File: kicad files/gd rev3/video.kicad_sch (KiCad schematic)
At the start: 51 parts, among them J17 VGA_Micro, J18 vga_SWD, J22 L77HDE15SD1CH4F, SW6 VGA Boot Sel, SW7 VGA RESET, U19 W25Q128JVS, U22 74HCT245, U23 RP2040, U24 74LVC2G04, Y2 ECS-120-18-33-JEM-TR

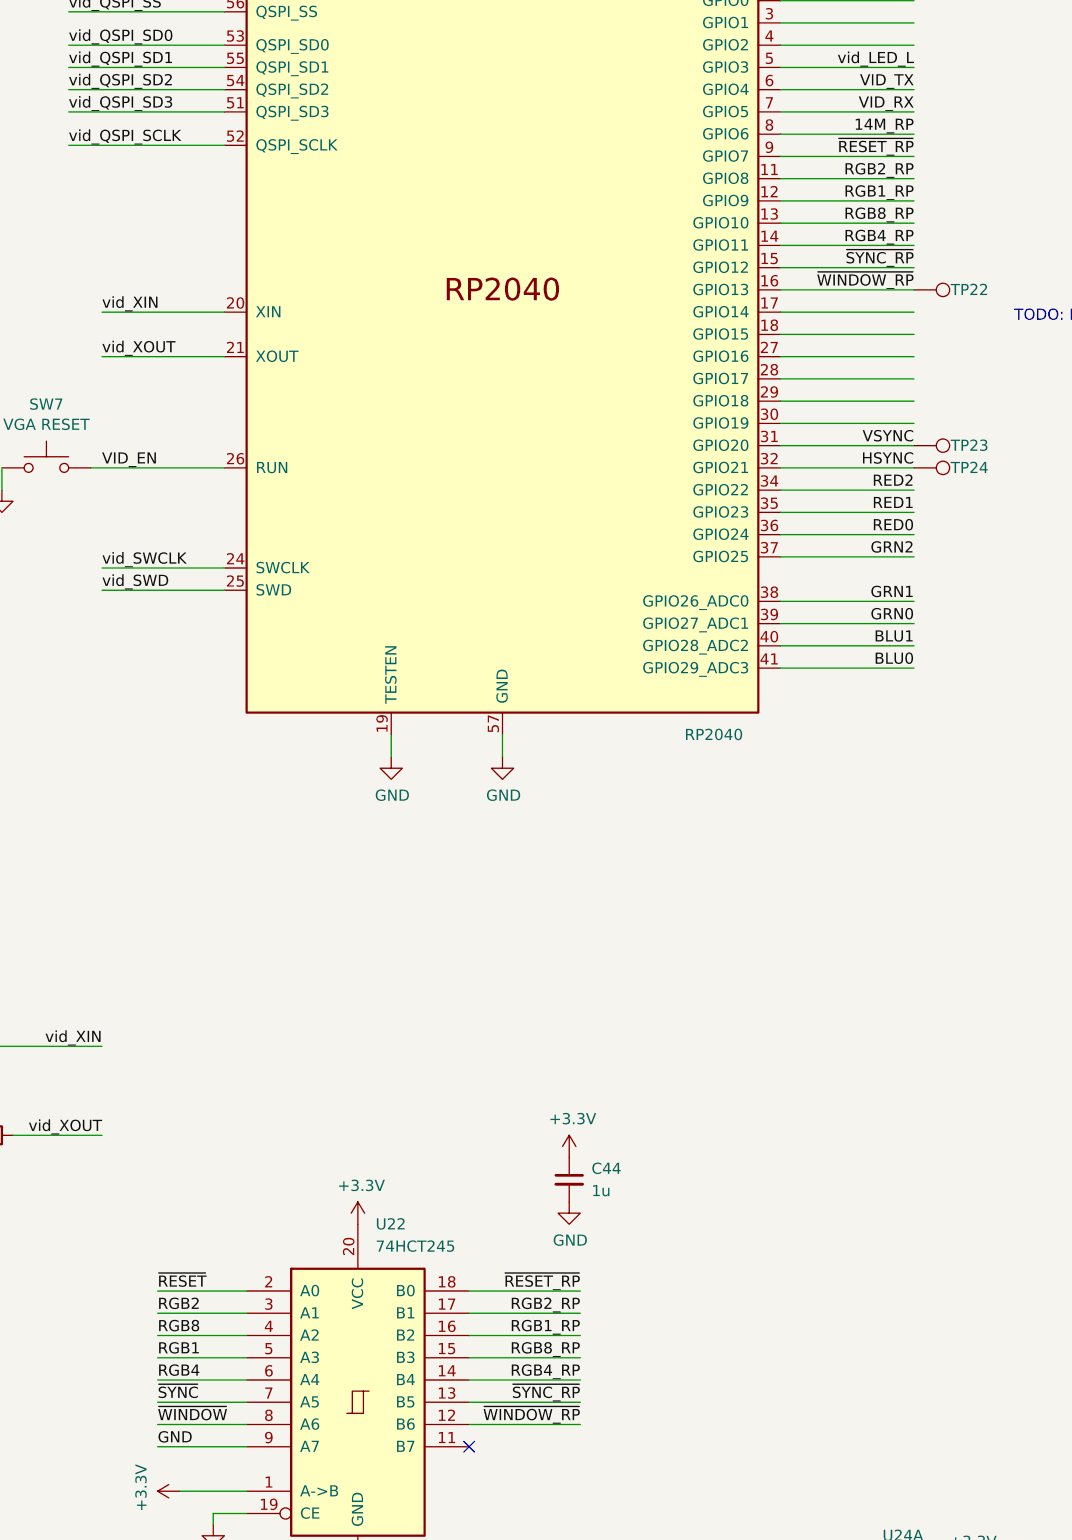
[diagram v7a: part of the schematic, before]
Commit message: made it smaller to make a buck
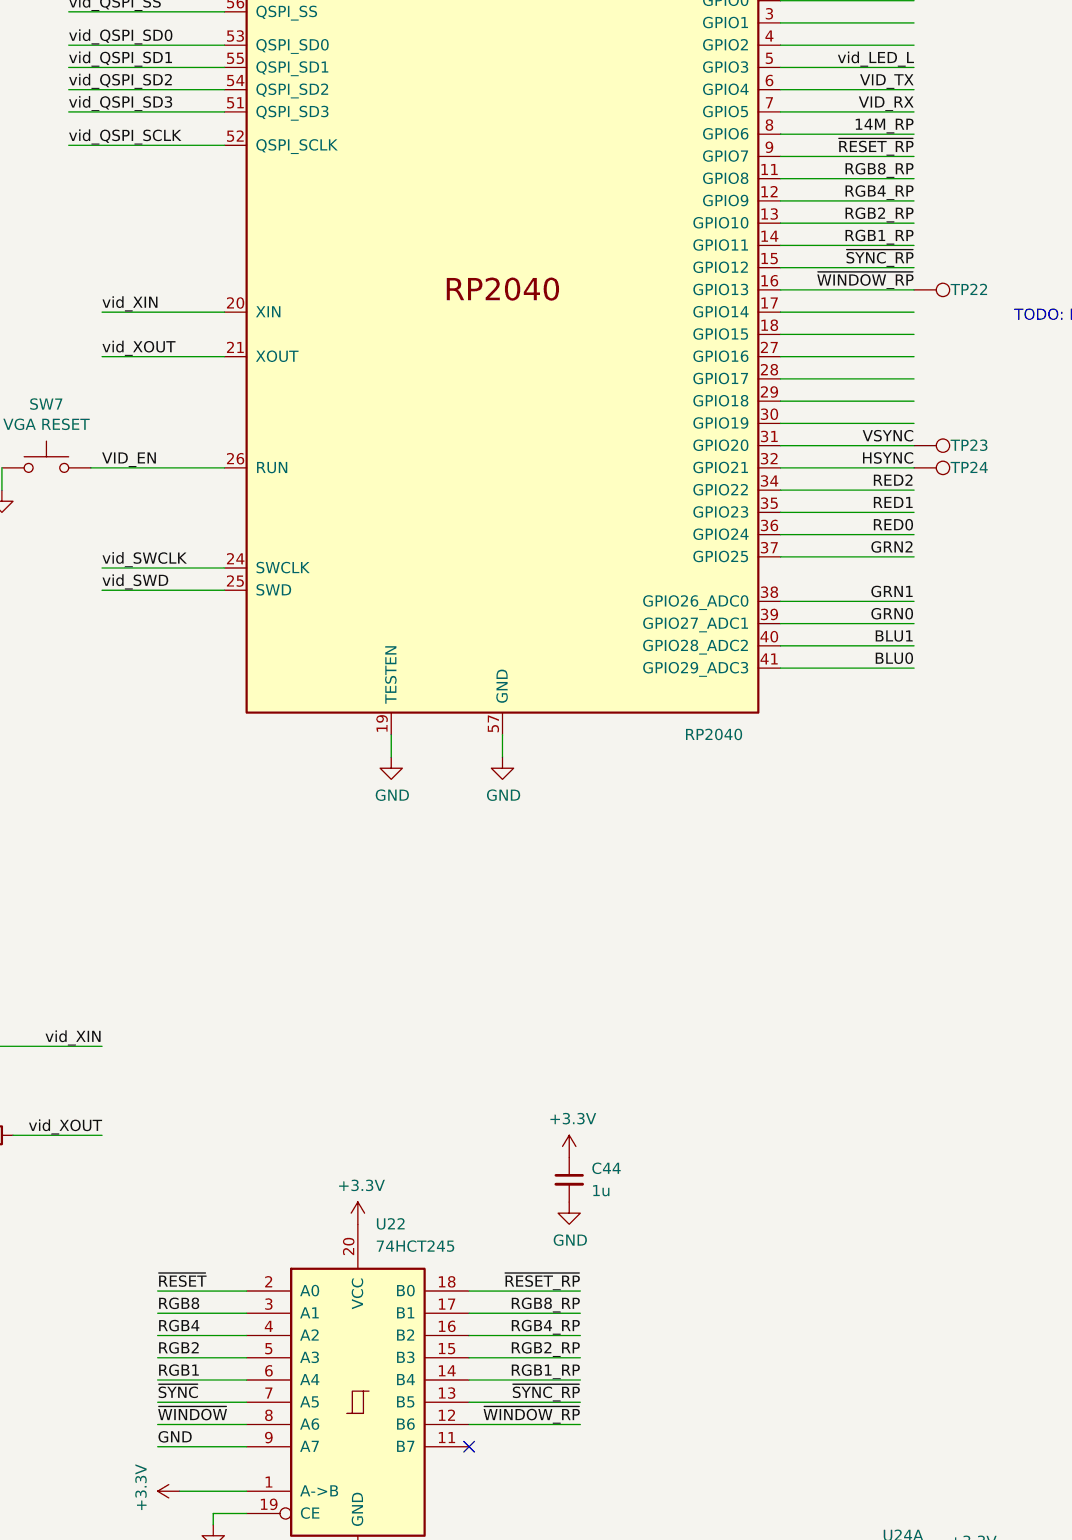
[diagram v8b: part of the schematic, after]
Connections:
- net RGB1: now also U22.6 (A4); no longer U22.5 (A3)
- net RGB1_RP: now also U22.14 (B4), U23.14 (GPIO11); no longer U22.16 (B2), U23.12 (GPIO9)
- net RGB2: now also U22.5 (A3); no longer U22.3 (A1)
- net RGB2_RP: now also U22.15 (B3), U23.13 (GPIO10); no longer U22.17 (B1), U23.11 (GPIO8)
- net RGB4: now also U22.4 (A2); no longer U22.6 (A4)
- net RGB4_RP: now also U22.16 (B2), U23.12 (GPIO9); no longer U22.14 (B4), U23.14 (GPIO11)
- net RGB8: now also U22.3 (A1); no longer U22.4 (A2)
- net RGB8_RP: now also U22.17 (B1), U23.11 (GPIO8); no longer U22.15 (B3), U23.13 (GPIO10)
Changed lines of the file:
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@@
     (effects (font (size 1.27 1.27)) (justify left bottom))
   )
-  (label "RGB4" (at 146.05 237.49 0)
+  (label "RGB4" (at 146.05 232.41 0)
     (effects (font (size 1.27 1.27)) (justify left bottom))
   )
@@
     (effects (font (size 1.27 1.27)) (justify left bottom))
   )
-  (label "RGB4_RP" (at 232.41 107.95 180)
+  (label "RGB4_RP" (at 232.41 102.87 180)
     (effects (font (size 1.27 1.27)) (justify right bottom))
   )
@@
     (effects (font (size 1.27 1.27)) (justify right bottom))
   )
-  (label "RGB1" (at 146.05 234.95 0)
+  (label "RGB1" (at 146.05 237.49 0)
     (effects (font (size 1.27 1.27)) (justify left bottom))
   )
@@
     (effects (font (size 1.27 1.27)) (justify right bottom))
   )
-  (label "RGB1_RP" (at 194.31 232.41 180)
+  (label "RGB1_RP" (at 194.31 237.49 180)
     (effects (font (size 1.27 1.27)) (justify right bottom))
   )
@@
     (effects (font (size 1.27 1.27)) (justify left bottom))
   )
-  (label "RGB4_RP" (at 194.31 237.49 180)
+  (label "RGB4_RP" (at 194.31 232.41 180)
     (effects (font (size 1.27 1.27)) (justify right bottom))
   )
@@
     (effects (font (size 1.27 1.27)) (justify left bottom))
   )
-  (label "RGB2" (at 146.05 229.87 0)
+  (label "RGB2" (at 146.05 234.95 0)
     (effects (font (size 1.27 1.27)) (justify left bottom))
   )
@@
     (effects (font (size 1.27 1.27)) (justify left bottom))
   )
-  (label "RGB8_RP" (at 232.41 105.41 180)
+  (label "RGB8_RP" (at 232.41 100.33 180)
     (effects (font (size 1.27 1.27)) (justify right bottom))
   )
@@
     (effects (font (size 1.27 1.27)) (justify left bottom))
   )
-  (label "RGB2_RP" (at 232.41 100.33 180)
+  (label "RGB2_RP" (at 232.41 105.41 180)
     (effects (font (size 1.27 1.27)) (justify right bottom))
   )
@@
     (effects (font (size 1.27 1.27)) (justify left bottom))
   )
-  (label "RGB8_RP" (at 194.31 234.95 180)
+  (label "RGB8_RP" (at 194.31 229.87 180)
     (effects (font (size 1.27 1.27)) (justify right bottom))
   )
@@
     (effects (font (size 1.27 1.27)) (justify right bottom))
   )
-  (label "RGB2_RP" (at 194.31 229.87 180)
+  (label "RGB2_RP" (at 194.31 234.95 180)
     (effects (font (size 1.27 1.27)) (justify right bottom))
   )
@@
     (effects (font (size 1.27 1.27)) (justify right bottom))
   )
-  (label "RGB8" (at 146.05 232.41 0)
-    (effects (font (size 1.27 1.27)) (justify left bottom))
-  )
-  (label "RGB1_RP" (at 232.41 102.87 180)
-    (effects (font (size 1.27 1.27)) (justify right bottom))
-  )
+  (label "RGB8" (at 146.05 229.87 0)
+    (effects (font (size 1.27 1.27)) (justify left bottom))
+  )
+  (label "RGB1_RP" (at 232.41 107.95 180)
+    (effects (font (size 1.27 1.27)) (justify right bottom))
+  )
